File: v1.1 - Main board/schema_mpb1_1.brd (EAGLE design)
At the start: 85.3 x 70.8 mm, 79 parts, among them IC1 CP2102, Q1 8M, Q2 32.768kHz, U1 NCP1117ST33T3G, U2 NCP1117ST50T3G, X2 PN61729-S, X5 POWERSUPPLY_DC21MMX

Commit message: COM board
- Routed first version of Wireless COM board
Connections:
- net NRF_CE renamed NRF_TX
- net NRF_CS renamed NRF_RX
- net NRF_IRQ renamed PB8
- net NRF_MISO renamed PB4
- net NRF_MOSI renamed ESP_RX
- net NRF_SCK renamed ESP_TX
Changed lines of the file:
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@@
 <contactref element="U$2" pad="65"/>
 </signal>
-<signal name="NRF_CE">
+<signal name="NRF_TX">
 <contactref element="U$2" pad="92"/>
 <contactref element="COM" pad="10"/>
@@
 <wire x1="58.0136" y1="65.8622" x2="59.182" y2="67.0306" width="0.1524" layer="16"/>
 </signal>
-<signal name="NRF_CS">
+<signal name="NRF_RX">
 <contactref element="U$2" pad="93"/>
 <contactref element="COM" pad="11"/>
@@
 <wire x1="57.6834" y1="40.1828" x2="61.6966" y2="44.196" width="0.1524" layer="16"/>
 </signal>
-<signal name="NRF_SCK">
+<signal name="ESP_TX">
 <contactref element="U$2" pad="89"/>
 <contactref element="JTAG" pad="6"/>
@@
 <wire x1="57.658" y1="27.432" x2="57.658" y2="26.67" width="0.1524" layer="16"/>
 </signal>
-<signal name="NRF_MOSI">
+<signal name="ESP_RX">
 <contactref element="U$2" pad="91"/>
 <contactref element="COM" pad="8"/>
@@
 <wire x1="58.1152" y1="61.976" x2="58.1152" y2="42.8752" width="0.1524" layer="16"/>
 </signal>
-<signal name="NRF_MISO">
+<signal name="PB4">
 <contactref element="U$2" pad="90"/>
 <contactref element="COM" pad="9"/>
@@
 <wire x1="57.4548" y1="36.5506" x2="67.564" y2="36.5506" width="0.1524" layer="1"/>
 </signal>
-<signal name="NRF_IRQ">
+<signal name="PB8">
 <contactref element="U$2" pad="95"/>
 <contactref element="COM" pad="12"/>

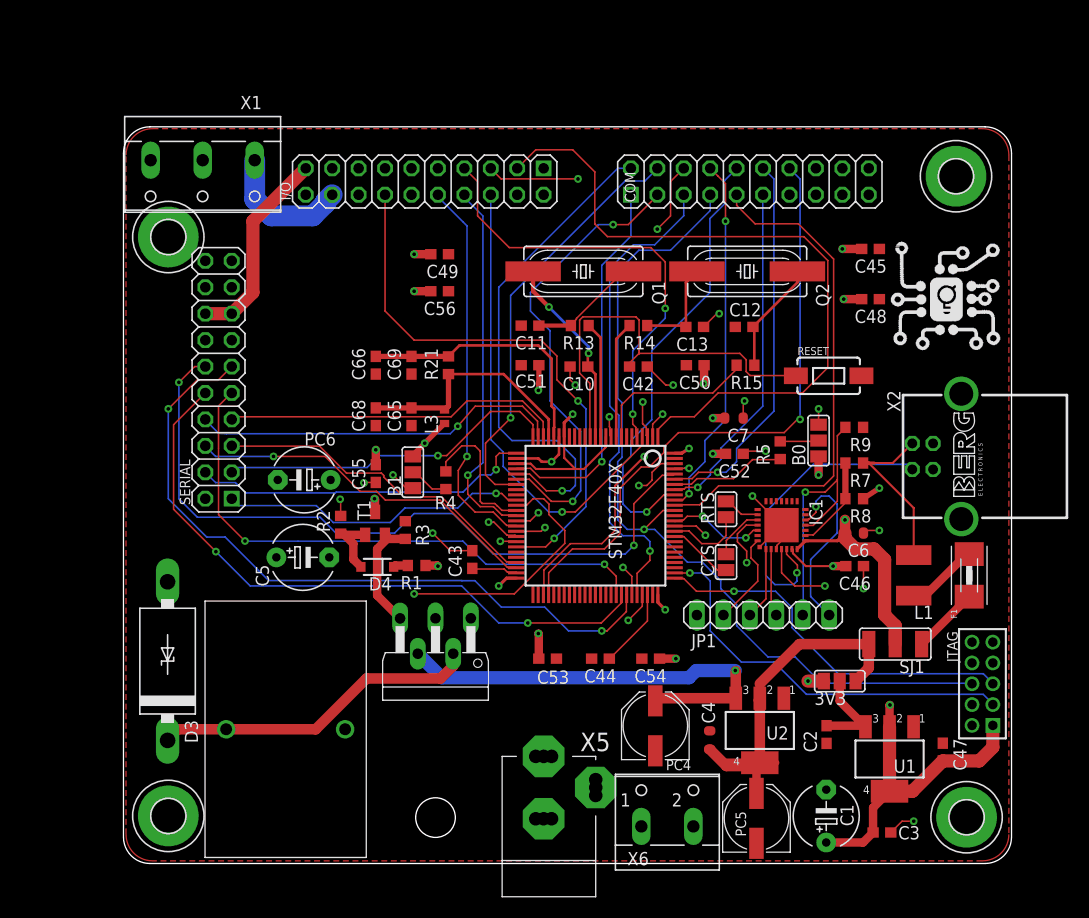
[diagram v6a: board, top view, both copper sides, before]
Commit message: Main board
Changed drill size of vias to 0.4mm
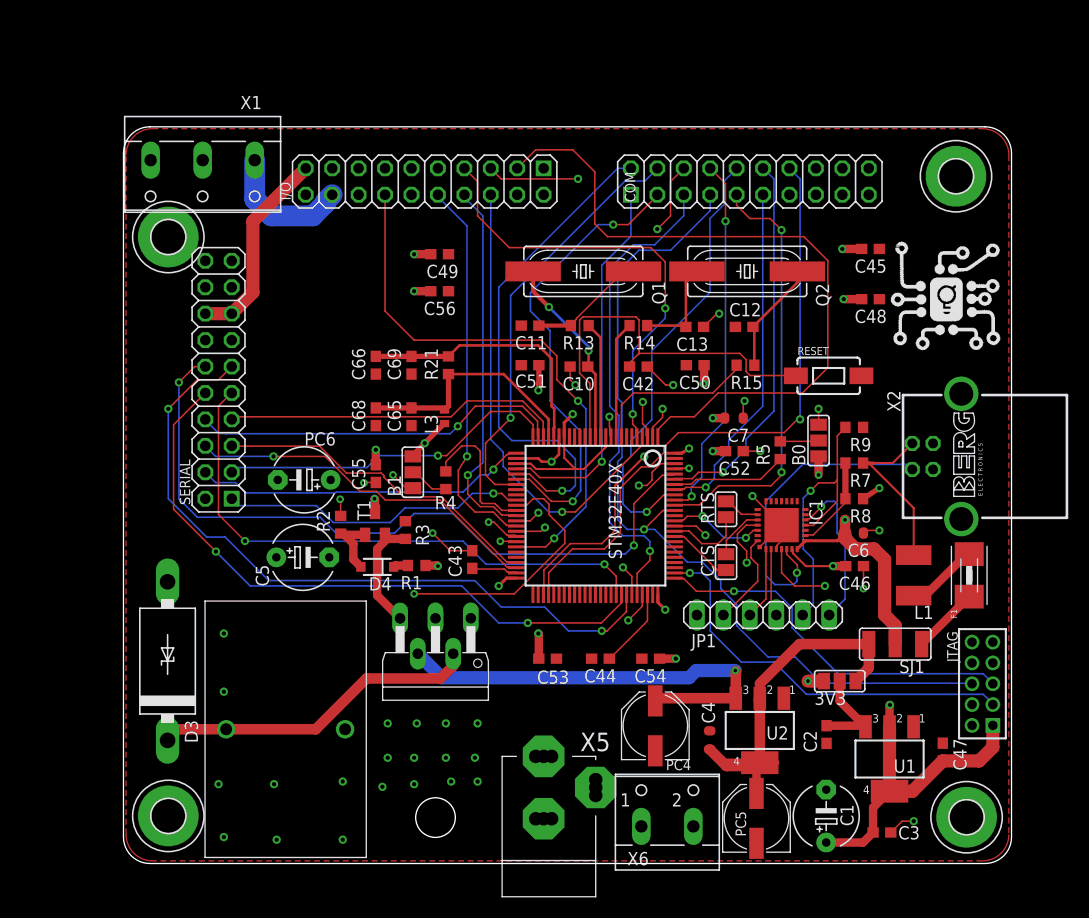
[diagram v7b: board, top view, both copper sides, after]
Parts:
- moved C52 0.25 mm to (59.0, 39.9)
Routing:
- net PB4: track 49.8 -> 41.4 mm, vias 0 -> 2
- net N$26: track 17.4 -> 15.5 mm
- net RX2: track 33.0 -> 32.4 mm
- net GND: track 48.8 -> 48.2 mm, vias 17 -> 37
- net N$13: track 29.3 -> 29.9 mm
- net N$21: track 27.0 -> 27.5 mm

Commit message: Main board
Applied ground stitching
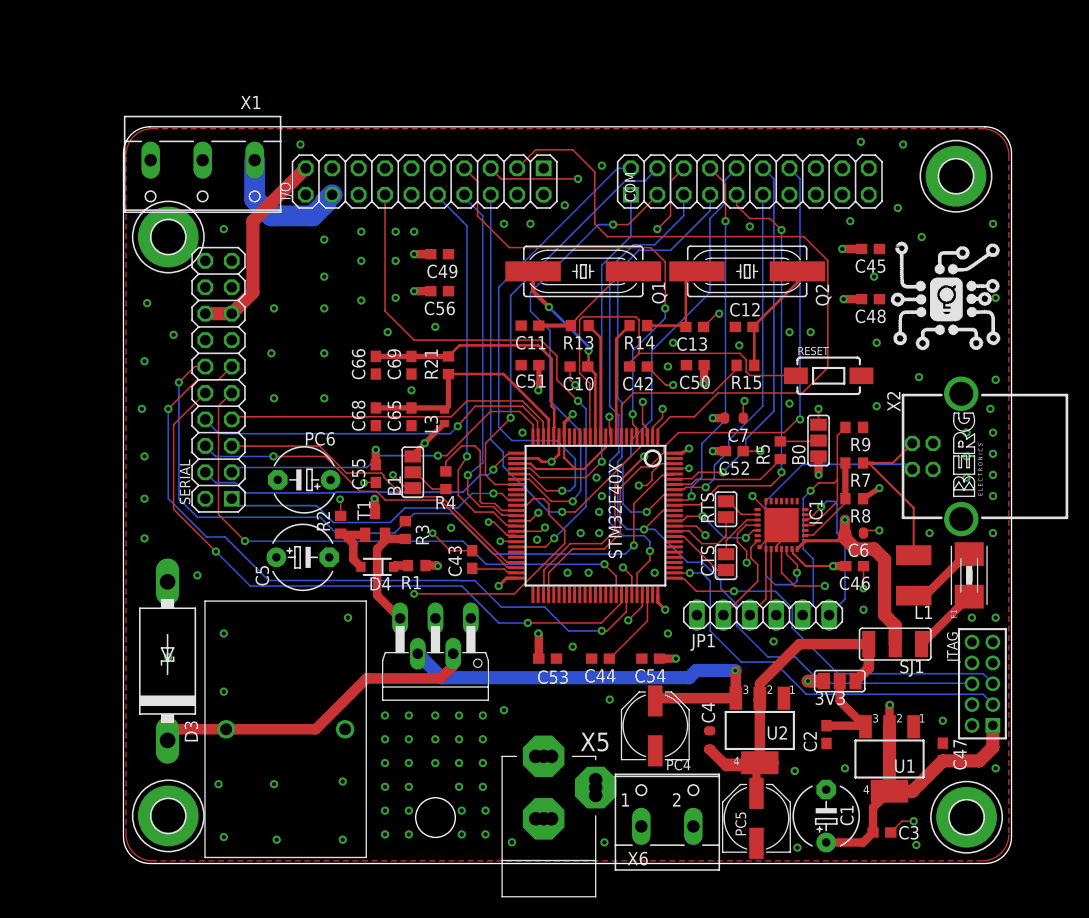
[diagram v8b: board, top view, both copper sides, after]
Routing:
- net GND: vias 37 -> 138
